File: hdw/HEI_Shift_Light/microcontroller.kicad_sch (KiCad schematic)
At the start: 17 parts

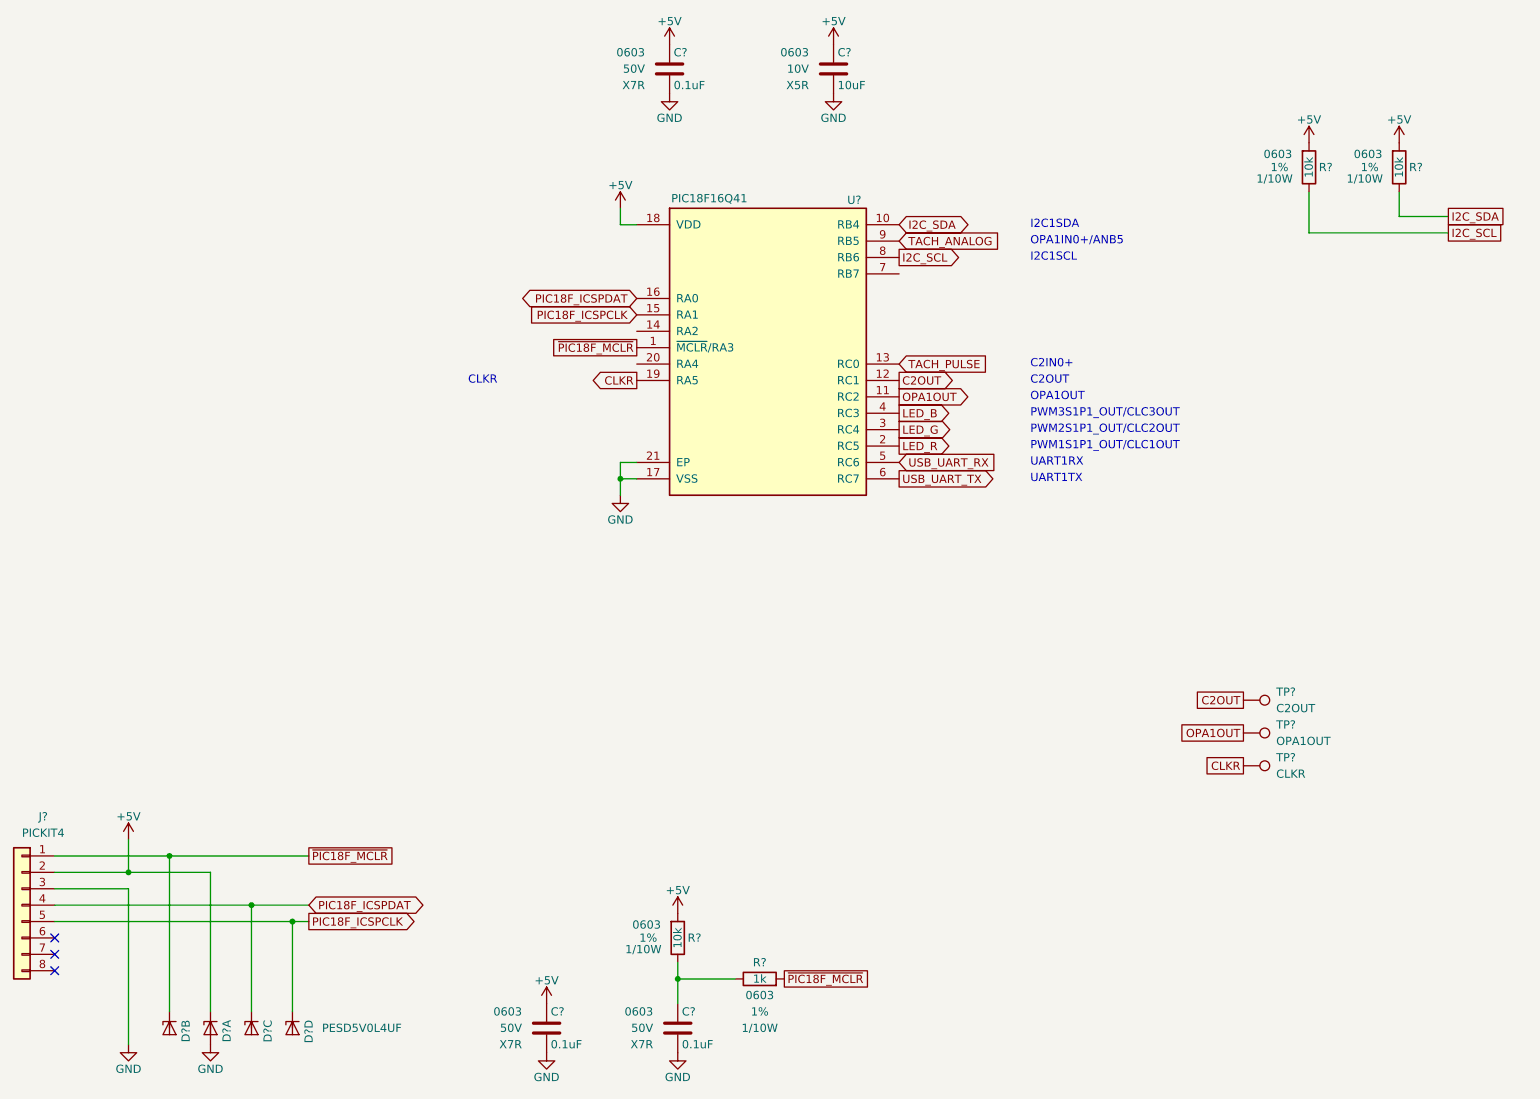
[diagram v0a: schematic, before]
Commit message: filled in digikey part numbers
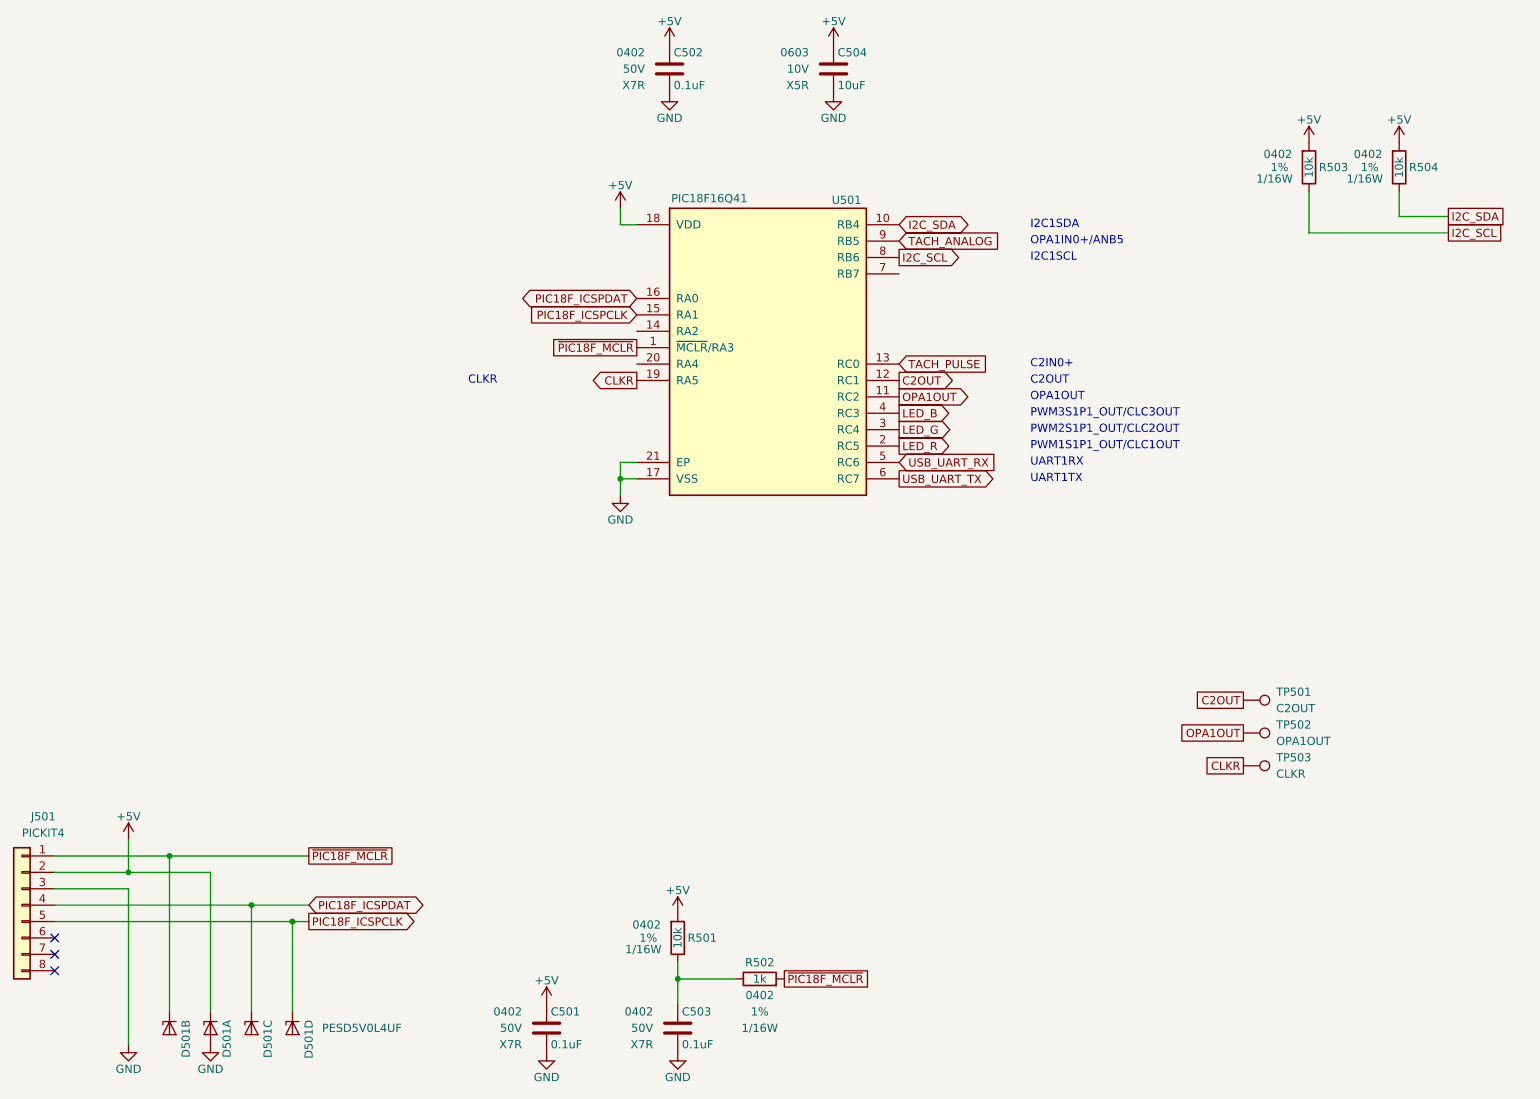
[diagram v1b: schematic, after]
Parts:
- C501, C503: renamed from C?; footprint Capacitors_SMD:C_0603 -> Capacitors_SMD:C_0402; Digi-Key PN 1276-1935-1-ND -> 399-7845-1-ND; display_footprint 0603 -> 0402
- C502: renamed from C?; footprint Capacitors_SMD:C_0603 -> Capacitors_SMD:C_0402; display_footprint 0603 -> 0402
- D501: renamed from D?; Digi-Key PN (none) -> 1727-5796-2-ND
- J501: renamed from J?; Digi-Key PN (none) -> SAM1051-08-ND
- R501, R503, R504: renamed from R?; footprint Resistors_SMD:R_0603 -> Resistors_SMD:R_0402; Digi-Key PN 541-10.0KHCT-ND -> 541-10.0KLCT-ND; Wattage 1/10W -> 1/16W; display_footprint 0603 -> 0402
- R502: renamed from R?; footprint Resistors_SMD:R_0603 -> Resistors_SMD:R_0402; Digi-Key PN 541-1.00KHCT-ND -> 541-1.00KLCT-ND; Wattage 1/10W -> 1/16W; display_footprint 0603 -> 0402
- U501: renamed from U?; Digi-Key PN (none) -> 150-PIC18F16Q41-I-REB-ND
- gave numbers to parts that had none: 5

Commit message: fixed some digikey pns
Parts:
- C501, C502, C503: Digi-Key PN 399-7845-1-ND -> 1276-7069-1-ND
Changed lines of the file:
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@@
 			)
 		)
-		(property "Digi-Key PN" "399-7845-1-ND"
+		(property "Digi-Key PN" "1276-7069-1-ND"
 			(at 109.855 173.99 0)
 			(hide yes)
@@
 			)
 		)
-		(property "Digi-Key PN" "399-7845-1-ND"
+		(property "Digi-Key PN" "1276-7069-1-ND"
 			(at 130.175 173.99 0)
 			(hide yes)
@@
 			)
 		)
-		(property "Digi-Key PN" "399-7845-1-ND"
+		(property "Digi-Key PN" "1276-7069-1-ND"
 			(at 128.905 25.4 0)
 			(hide yes)

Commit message: added component datasheet properties
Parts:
- C501, C502, C503: Digi-Key PN 1276-7069-1-ND -> 445-5932-1-ND
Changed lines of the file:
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@@
 			)
 		)
-		(property "Datasheet" ""
+		(property "Datasheet" "https://www.vishay.com/docs/20035/dcrcwe3.pdf"
 			(at 217.17 53.34 0)
 			(hide yes)
@@
 			)
 		)
-		(property "Datasheet" ""
+		(property "Datasheet" "https://www.vishay.com/docs/20035/dcrcwe3.pdf"
 			(at 132.08 179.07 0)
 			(hide yes)
@@
 			)
 		)
-		(property "Datasheet" ""
+		(property "Datasheet" "https://www.vishay.com/docs/20035/dcrcwe3.pdf"
 			(at 119.38 172.72 0)
 			(hide yes)
@@
 			)
 		)
-		(property "Datasheet" ""
+		(property "Datasheet" "https://product.tdk.com/en/system/files/dam/doc/product/capacitor/ceramic/mlcc/charasheet/c1005x7r1h104k050bb.pdf"
 			(at 99.695 184.15 0)
 			(hide yes)
@@
 			)
 		)
-		(property "Digi-Key PN" "1276-7069-1-ND"
+		(property "Digi-Key PN" "445-5932-1-ND"
 			(at 109.855 173.99 0)
 			(hide yes)
@@
 			)
 		)
-		(property "Datasheet" ""
+		(property "Datasheet" "https://product.tdk.com/en/system/files/dam/doc/product/capacitor/ceramic/mlcc/charasheet/c1005x7r1h104k050bb.pdf"
 			(at 120.015 184.15 0)
 			(hide yes)
@@
 			)
 		)
-		(property "Digi-Key PN" "1276-7069-1-ND"
+		(property "Digi-Key PN" "445-5932-1-ND"
 			(at 130.175 173.99 0)
 			(hide yes)
@@
 			)
 		)
-		(property "Datasheet" ""
+		(property "Datasheet" "https://product.tdk.com/en/system/files/dam/doc/product/capacitor/ceramic/mlcc/charasheet/c1005x7r1h104k050bb.pdf"
 			(at 118.745 35.56 0)
 			(hide yes)
@@
 			)
 		)
-		(property "Digi-Key PN" "1276-7069-1-ND"
+		(property "Digi-Key PN" "445-5932-1-ND"
 			(at 128.905 25.4 0)
 			(hide yes)
@@
 			)
 		)
-		(property "Datasheet" ""
+		(property "Datasheet" "https://search.murata.co.jp/Ceramy/image/img/A01X/G101/ENG/GRM188R61A106KE69-01.pdf"
 			(at 144.145 35.56 0)
 			(hide yes)
@@
 			)
 		)
-		(property "Datasheet" ""
+		(property "Datasheet" "https://suddendocs.samtec.com/catalog_english/htsw_th.pdf"
 			(at 17.78 167.64 0)
 			(hide yes)
@@
 			)
 		)
-		(property "Datasheet" ""
+		(property "Datasheet" "https://www.vishay.com/docs/20035/dcrcwe3.pdf"
 			(at 231.14 53.34 0)
 			(hide yes)

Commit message: cleaned up digikey pns
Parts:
- C504: Digi-Key PN 490-10474-1-ND -> 445-C1608X5R1A106K080ACCT-ND
- D501: Digi-Key PN 1727-5796-2-ND -> 1727-5796-1-ND
- D501: Digi-Key PN (none) -> 1727-5796-1-ND
- U501: Digi-Key PN 150-PIC18F16Q41-I-REB-ND -> 150-PIC18F16Q41-I/REB-ND
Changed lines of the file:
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@@
 		(property "Intersheetrefs" "${INTERSHEET_REFS}"
 			(at 169.4158 64.77 0)
-			(hide yes)
 			(show_name no)
 			(do_not_autoplace no)
@@
 		(property "Intersheetrefs" "${INTERSHEET_REFS}"
 			(at 80.7576 170.18 0)
-			(hide yes)
 			(show_name no)
 			(do_not_autoplace no)
@@
 		(property "Intersheetrefs" "${INTERSHEET_REFS}"
 			(at 196.6089 140.97 0)
-			(hide yes)
 			(show_name no)
 			(do_not_autoplace no)
@@
 		(property "Intersheetrefs" "${INTERSHEET_REFS}"
 			(at 81.627 167.64 0)
-			(hide yes)
 			(show_name no)
 			(do_not_autoplace no)
@@
 		(property "Intersheetrefs" "${INTERSHEET_REFS}"
 			(at 94.5024 76.2 0)
-			(hide yes)
 			(show_name no)
 			(do_not_autoplace no)
@@
 		(property "Intersheetrefs" "${INTERSHEET_REFS}"
 			(at 105.2067 86.36 0)
-			(hide yes)
 			(show_name no)
 			(do_not_autoplace no)
@@
 		(property "Intersheetrefs" "${INTERSHEET_REFS}"
 			(at 98.5166 81.28 0)
-			(hide yes)
 			(show_name no)
 			(do_not_autoplace no)
@@
 		(property "Intersheetrefs" "${INTERSHEET_REFS}"
 			(at 93.633 73.66 0)
-			(hide yes)
 			(show_name no)
 			(do_not_autoplace no)
@@
 		(property "Intersheetrefs" "${INTERSHEET_REFS}"
 			(at 162.3399 91.44 0)
-			(hide yes)
 			(show_name no)
 			(do_not_autoplace no)
@@
 		(property "Intersheetrefs" "${INTERSHEET_REFS}"
 			(at 162.3399 96.52 0)
-			(hide yes)
 			(show_name no)
 			(do_not_autoplace no)
@@
 		(property "Intersheetrefs" "${INTERSHEET_REFS}"
 			(at 165.3865 62.23 0)
-			(hide yes)
 			(show_name no)
 			(do_not_autoplace no)
@@
 		(property "Intersheetrefs" "${INTERSHEET_REFS}"
 			(at 76.7434 160.02 0)
-			(hide yes)
 			(show_name no)
 			(do_not_autoplace no)
@@
 		(property "Intersheetrefs" "${INTERSHEET_REFS}"
 			(at 165.1824 88.9 0)
-			(hide yes)
 			(show_name no)
 			(do_not_autoplace no)
@@
 		(property "Intersheetrefs" "${INTERSHEET_REFS}"
 			(at 168.2666 83.82 0)
-			(hide yes)
 			(show_name no)
 			(do_not_autoplace no)
@@
 		(property "Intersheetrefs" "${INTERSHEET_REFS}"
 			(at 162.3399 93.98 0)
-			(hide yes)
 			(show_name no)
 			(do_not_autoplace no)
@@
 		(property "Intersheetrefs" "${INTERSHEET_REFS}"
 			(at 248.1934 63.5 0)
-			(hide yes)
 			(show_name no)
 			(do_not_autoplace no)
@@
 		(property "Intersheetrefs" "${INTERSHEET_REFS}"
 			(at 169.2342 101.6 0)
-			(hide yes)
 			(show_name no)
 			(do_not_autoplace no)
@@
 		(property "Intersheetrefs" "${INTERSHEET_REFS}"
 			(at 248.2539 60.96 0)
-			(hide yes)
 			(show_name no)
 			(do_not_autoplace no)
@@
 		(property "Intersheetrefs" "${INTERSHEET_REFS}"
 			(at 164.2147 67.31 0)
-			(hide yes)
 			(show_name no)
 			(do_not_autoplace no)
@@
 		(property "Intersheetrefs" "${INTERSHEET_REFS}"
 			(at 200.298 146.05 0)
-			(hide yes)
 			(show_name no)
 			(do_not_autoplace no)
@@
 		(property "Intersheetrefs" "${INTERSHEET_REFS}"
 			(at 150.4034 179.07 0)
-			(hide yes)
 			(show_name no)
 			(do_not_autoplace no)
@@
 		(property "Intersheetrefs" "${INTERSHEET_REFS}"
 			(at 169.5366 99.06 0)
-			(hide yes)
 			(show_name no)
 			(do_not_autoplace no)
@@
 		(property "Intersheetrefs" "${INTERSHEET_REFS}"
 			(at 162.7633 86.36 0)
-			(hide yes)
 			(show_name no)
 			(do_not_autoplace no)
@@
 		(property "Intersheetrefs" "${INTERSHEET_REFS}"
 			(at 199.028 135.89 0)
-			(hide yes)
 			(show_name no)
 			(do_not_autoplace no)
@@
 			)
 		)
-		(property "Digi-Key PN" "1727-5796-2-ND"
+		(property "Digi-Key PN" "1727-5796-1-ND"
 			(at 40.64 186.69 0)
 			(hide yes)
@@
 			)
 		)
-		(property "Digi-Key PN" "150-PIC18F16Q41-I-REB-ND"
+		(property "Digi-Key PN" "150-PIC18F16Q41-I/REB-ND"
 			(at 133.35 81.28 0)
 			(hide yes)
@@
 			)
 		)
+		(property "Digi-Key PN" "1727-5796-1-ND"
+			(at 53.34 186.69 0)
+			(hide yes)
+			(show_name no)
+			(do_not_autoplace no)
+			(effects
+				(font
+					(size 1.27 1.27)
+				)
+			)
+		)
 		(pin "6"
 		)
@@
 			)
 		)
-		(property "Digi-Key PN" "490-10474-1-ND"
+		(property "Digi-Key PN" "445-C1608X5R1A106K080ACCT-ND"
 			(at 143.51 38.1 0)
 			(hide yes)
@@
 			)
 		)
+		(property "Digi-Key PN" "1727-5796-1-ND"
+			(at 46.99 186.69 0)
+			(hide yes)
+			(show_name no)
+			(do_not_autoplace no)
+			(effects
+				(font
+					(size 1.27 1.27)
+				)
+			)
+		)
 		(pin "6"
 		)
@@
 			(at 59.69 186.69 0)
 			(hide yes)
+			(show_name no)
+			(do_not_autoplace no)
+			(effects
+				(font
+					(size 1.27 1.27)
+				)
+			)
+		)
+		(property "Digi-Key PN" "1727-5796-1-ND"
+			(at 59.69 186.69 0)
+			(hide yes)

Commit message: fixed some footprints, pulled into PCB
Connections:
- net POS5_PGOOD: now reaches U501.7 (RB7)
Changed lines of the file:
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@@
+		)
+	)
+	(global_label "POS5_PGOOD"
+		(shape input)
+		(at 153.67 69.85 0)
+		(fields_autoplaced yes)
+		(effects
+			(font
+				(size 1.27 1.27)
+			)
+			(justify left)
+		)
+		(property "Intersheetrefs" "${INTERSHEET_REFS}"
+			(at 169.1133 69.85 0)
+			(show_name no)
+			(do_not_autoplace no)
+			(effects
+				(font
+					(size 1.27 1.27)
+				)
+				(justify left)
+			)
 		)
 	)

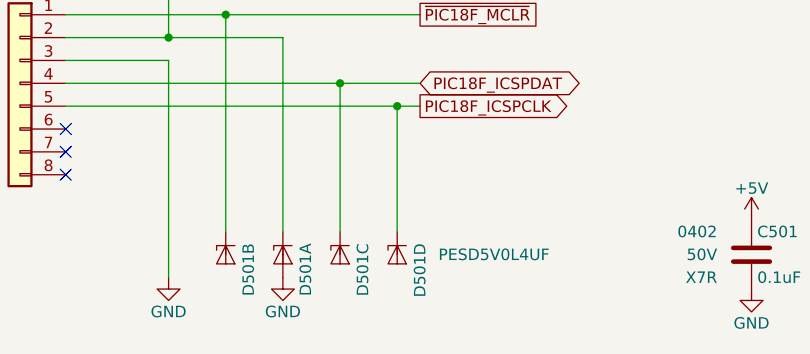
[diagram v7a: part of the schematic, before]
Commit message: routed most of board
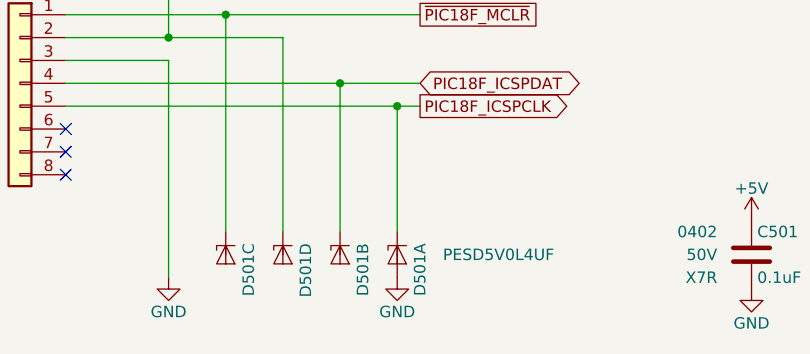
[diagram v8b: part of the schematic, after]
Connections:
- net +5V: now also D501.6 (K4); no longer D501.1 (K1)
- net PIC18F_ICSPCLK: now also D501.1 (K1); no longer D501.6 (K4)
- net PIC18F_ICSPDAT: now also D501.3 (K2); no longer D501.4 (K3)
- net ~{PIC18F_MCLR}: now also D501.4 (K3); no longer D501.3 (K2)
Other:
- moved on the sheet: D501A, D501B, D501C, D501D
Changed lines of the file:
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@@
 	(symbol
 		(lib_id "power:GND")
-		(at 46.99 189.23 0)
+		(at 59.69 189.23 0)
 		(mirror y)
 		(unit 1)
@@
 		(dnp no)
 		(property "Reference" "#PWR0503"
-			(at 46.99 195.58 0)
+			(at 59.69 195.58 0)
 			(hide yes)
 			(show_name no)
@@
 		)
 		(property "Value" "GND"
-			(at 46.99 193.04 0)
+			(at 59.69 193.04 0)
 			(show_name no)
 			(do_not_autoplace no)
@@
 		)
 		(property "Footprint" ""
-			(at 46.99 189.23 0)
+			(at 59.69 189.23 0)
 			(hide yes)
 			(show_name no)
@@
 		)
 		(property "Datasheet" ""
-			(at 46.99 189.23 0)
+			(at 59.69 189.23 0)
 			(hide yes)
 			(show_name no)
@@
 		)
 		(property "Description" ""
-			(at 46.99 189.23 0)
+			(at 59.69 189.23 0)
 			(show_name no)
 			(do_not_autoplace no)
@@
 	(symbol
 		(lib_id "Power_Protection:PESD5V0L4UF")
-		(at 40.64 186.69 270)
+		(at 53.34 186.69 270)
 		(unit 2)
 		(body_style 1)
@@
 		(dnp no)
 		(property "Reference" "D501"
-			(at 43.18 185.4199 0)
+			(at 55.88 185.4199 0)
 			(show_name no)
 			(do_not_autoplace no)
@@
 		)
 		(property "Value" "PESD5V0L4UF"
-			(at 64.262 186.69 90)
+			(at 76.962 186.69 90)
 			(hide yes)
 			(show_name no)
@@
 		)
 		(property "Footprint" "Package_TO_SOT_SMD:SOT-886"
-			(at 45.72 186.69 0)
+			(at 58.42 186.69 0)
 			(hide yes)
 			(show_name no)
@@
 		)
 		(property "Datasheet" "https://assets.nexperia.com/documents/data-sheet/PESDXL4UF_G_W.pdf"
-			(at 35.56 186.69 0)
+			(at 48.26 186.69 0)
 			(hide yes)
 			(show_name no)
@@
 		)
 		(property "Description" "Low capacitance unidirectional quadruple ESD protection diode array, 5.0V, Common Anode, SOT-886"
-			(at 40.64 186.69 0)
+			(at 53.34 186.69 0)
 			(hide yes)
 			(show_name no)
@@
 		)
 		(property "Digi-Key PN" "1727-5796-1-ND"
-			(at 40.64 186.69 0)
+			(at 53.34 186.69 0)
 			(hide yes)
 			(show_name no)
@@
 	(symbol
 		(lib_id "Power_Protection:PESD5V0L4UF")
-		(at 53.34 186.69 270)
+		(at 40.64 186.69 270)
 		(unit 3)
 		(body_style 1)
@@
 		(dnp no)
 		(property "Reference" "D501"
-			(at 55.88 185.4199 0)
+			(at 43.18 185.4199 0)
 			(show_name no)
 			(do_not_autoplace no)
@@
 		)
 		(property "Value" "PESD5V0L4UF"
-			(at 76.962 186.69 90)
+			(at 64.262 186.69 90)
 			(hide yes)
 			(show_name no)
@@
 		)
 		(property "Footprint" "Package_TO_SOT_SMD:SOT-886"
-			(at 58.42 186.69 0)
+			(at 45.72 186.69 0)
 			(hide yes)
 			(show_name no)
@@
 		)
 		(property "Datasheet" "https://assets.nexperia.com/documents/data-sheet/PESDXL4UF_G_W.pdf"
-			(at 48.26 186.69 0)
+			(at 35.56 186.69 0)
 			(hide yes)
 			(show_name no)
@@
 		)
 		(property "Description" "Low capacitance unidirectional quadruple ESD protection diode array, 5.0V, Common Anode, SOT-886"
-			(at 53.34 186.69 0)
+			(at 40.64 186.69 0)
 			(hide yes)
 			(show_name no)
@@
 		)
 		(property "Digi-Key PN" "1727-5796-1-ND"
-			(at 53.34 186.69 0)
+			(at 40.64 186.69 0)
 			(hide yes)
 			(show_name no)
@@
 	(symbol
 		(lib_id "Power_Protection:PESD5V0L4UF")
-		(at 46.99 186.69 270)
+		(at 59.69 186.69 270)
 		(unit 1)
 		(body_style 1)
@@
 		(dnp no)
 		(property "Reference" "D501"
-			(at 49.53 185.4199 0)
+			(at 62.23 185.4199 0)
 			(show_name no)
 			(do_not_autoplace no)
@@
 		)
 		(property "Value" "PESD5V0L4UF"
-			(at 64.262 186.69 90)
+			(at 64.77 186.69 90)
 			(show_name no)
 			(do_not_autoplace no)
@@
 		)
 		(property "Footprint" "Package_TO_SOT_SMD:SOT-886"
-			(at 52.07 186.69 0)
+			(at 64.77 186.69 0)
 			(hide yes)
 			(show_name no)
@@
 		)
 		(property "Datasheet" "https://assets.nexperia.com/documents/data-sheet/PESDXL4UF_G_W.pdf"
-			(at 41.91 186.69 0)
+			(at 54.61 186.69 0)
 			(hide yes)
 			(show_name no)
@@
 		)
 		(property "Description" "Low capacitance unidirectional quadruple ESD protection diode array, 5.0V, Common Anode, SOT-886"
-			(at 46.99 186.69 0)
+			(at 59.69 186.69 0)
 			(hide yes)
 			(show_name no)
@@
 		)
 		(property "Digi-Key PN" "1727-5796-1-ND"
-			(at 46.99 186.69 0)
+			(at 59.69 186.69 0)
 			(hide yes)
 			(show_name no)
@@
 	(symbol
 		(lib_id "Power_Protection:PESD5V0L4UF")
-		(at 59.69 186.69 270)
+		(at 46.99 186.69 270)
 		(unit 4)
 		(body_style 1)
@@
 		(dnp no)
 		(property "Reference" "D501"
-			(at 62.23 185.4199 0)
+			(at 49.53 185.4199 0)
 			(show_name no)
 			(do_not_autoplace no)
@@
 		)
 		(property "Value" "PESD5V0L4UF"
-			(at 83.312 186.69 90)
+			(at 70.612 186.69 90)
 			(hide yes)
 			(show_name no)
@@
 		)
 		(property "Footprint" "Package_TO_SOT_SMD:SOT-886"
-			(at 64.77 186.69 0)
+			(at 52.07 186.69 0)
 			(hide yes)
 			(show_name no)
@@
 		)
 		(property "Datasheet" "https://assets.nexperia.com/documents/data-sheet/PESDXL4UF_G_W.pdf"
-			(at 54.61 186.69 0)
+			(at 41.91 186.69 0)
 			(hide yes)
 			(show_name no)
@@
 		)
 		(property "Description" "Low capacitance unidirectional quadruple ESD protection diode array, 5.0V, Common Anode, SOT-886"
-			(at 59.69 186.69 0)
+			(at 46.99 186.69 0)
 			(hide yes)
 			(show_name no)
@@
 		)
 		(property "Digi-Key PN" "1727-5796-1-ND"
-			(at 59.69 186.69 0)
-			(hide yes)
-			(show_name no)
+			(at 46.99 186.69 0)
+			(hide yes)
+			(show_name no)
